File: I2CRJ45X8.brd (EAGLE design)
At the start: 80 x 50 mm, 51 parts, among them IC1 MCP23017SO, IC2 MCP23017SO, J1 M06-SOCKET, J2 M06-SOCKET, J3 M02X3-PIN, J4 M02X3-PIN

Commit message: Board and schematic labelling
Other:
- board text added: "!INT"
- board text added: "(C)2019 SuperHouse Automation Pty Ltd Released under the terms of the TAPR Open Hardware License: www.tapr.org/OHL"
- board text added: "1: Data 1 2: Data 2 3: Data 3 4: VIN 5: VIN 6: Data 4 7: GND 8: GND"
- board text added: "1K in series with data lines"
- board text added: "8 Channel I2C RJ45 Breakout"
- board text added: "RJ45 Pinout"
- board text added: "Super House"
- board text added: "VCC:1.8-5.5V VIN:12V I2C Addr: 0x20-0x27"
- board text added: "by Jon Oxer"
- board text added: "superhouse.tv"
- board text added: "www.superhouse.tv/i2crj45x8"
- board text removed: "(C)2019 SuperHouse Automation Pty Ltd"
- board text removed: "INT"
- board text removed: "www.superhouse.tv/switchcontroller"
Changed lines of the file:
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@@
 <?xml version="1.0" encoding="utf-8"?>
 <!DOCTYPE eagle SYSTEM "eagle.dtd">
-<eagle version="9.4.2">
+<eagle version="9.5.0">
 <drawing>
 <settings>
@@
 <wire x1="80" y1="3" x2="77" y2="0" width="0" layer="20" curve="-90"/>
 <wire x1="77" y1="0" x2="3" y2="0" width="0" layer="20"/>
-<text x="0.953" y="8.123" size="1.0668" layer="21" font="vector" ratio="17">v1.0</text>
-<text x="20.955" y="2.854" size="1.27" layer="21" font="vector" ratio="17">www.superhouse.tv/switchcontroller</text>
-<text x="20.471" y="9.096" size="1.016" layer="21" font="vector" ratio="15" rot="SR0">(C)2019 SuperHouse Automation Pty Ltd</text>
-<text x="1.191" y="6.171" size="0.8128" layer="21" font="vector" ratio="17">SKU: I2CRJ45X8</text>
+<text x="71.953" y="4.123" size="1.0668" layer="21" font="vector" ratio="17">v1.0</text>
+<text x="17.5" y="48.6" size="1.016" layer="21" font="vector" ratio="17">www.superhouse.tv/i2crj45x8</text>
+<text x="61.471" y="1.096" size="1.27" layer="22" font="vector" ratio="15" rot="SMR0">(C)2019 SuperHouse Automation Pty Ltd
+Released under the terms of
+the TAPR Open Hardware License:
+www.tapr.org/OHL</text>
+<text x="7.829" y="2.191" size="1.016" layer="21" font="vector" ratio="17" rot="R90">SKU: I2CRJ45X8</text>
 <hole x="3" y="3" drill="3.2"/>
 <hole x="77" y="3" drill="3.2"/>
@@
 <text x="3.7" y="22.38" size="1.778" layer="21" font="vector" ratio="18" align="center-left">GND</text>
 <text x="3.7" y="19.84" size="1.778" layer="21" font="vector" ratio="18" align="center-left">VIN</text>
-<text x="3.7" y="17.3" size="1.778" layer="21" font="vector" ratio="18" align="center-left">INT</text>
+<text x="3.7" y="17.3" size="1.778" layer="21" font="vector" ratio="18" align="center-left">!INT</text>
 <text x="76.7" y="30" size="1.778" layer="21" font="vector" ratio="18" align="center-right">SDA</text>
 <text x="76.7" y="27.46" size="1.778" layer="21" font="vector" ratio="18" align="center-right">SCL</text>
@@
 <text x="76.7" y="22.38" size="1.778" layer="21" font="vector" ratio="18" align="center-right">GND</text>
 <text x="76.7" y="19.84" size="1.778" layer="21" font="vector" ratio="18" align="center-right">VIN</text>
-<text x="76.7" y="17.3" size="1.778" layer="21" font="vector" ratio="18" align="center-right">INT</text>
+<text x="76.7" y="17.3" size="1.778" layer="21" font="vector" ratio="18" align="center-right">!INT</text>
 <text x="75" y="13" size="1.27" layer="21" font="vector" ratio="18" align="center-left">VIN</text>
 <text x="75" y="10" size="1.27" layer="21" font="vector" ratio="18" align="center-left">VCC</text>
@@
 <wire x1="79" y1="10" x2="78" y2="11" width="0.254" layer="21" curve="90"/>
 <wire x1="78" y1="11" x2="72" y2="11" width="0.254" layer="21"/>
+<text x="30" y="26" size="1.6764" layer="22" font="vector" ratio="12" rot="MR0">1: Data 1
+2: Data 2
+3: Data 3
+4: VIN
+5: VIN
+6: Data 4
+7: GND
+8: GND</text>
+<text x="31.8" y="46" size="1.6764" layer="22" font="vector" ratio="16" rot="MR0">RJ45 Pinout</text>
+<wire x1="31" y1="49" x2="33" y2="47" width="0.254" layer="22" curve="-90"/>
+<wire x1="33" y1="47" x2="33" y2="27" width="0.254" layer="22"/>
+<wire x1="33" y1="27" x2="31" y2="25" width="0.254" layer="22" curve="-90"/>
+<wire x1="31" y1="25" x2="17" y2="25" width="0.254" layer="22"/>
+<wire x1="17" y1="25" x2="15" y2="27" width="0.254" layer="22" curve="-90"/>
+<wire x1="15" y1="47" x2="17" y2="49" width="0.254" layer="22" curve="-90"/>
+<wire x1="17" y1="49" x2="31" y2="49" width="0.254" layer="22"/>
+<wire x1="15" y1="47" x2="15" y2="27" width="0.254" layer="22"/>
+<text x="64.529" y="25.096" size="1.27" layer="22" font="vector" ratio="15" rot="SMR0">1K in series with data lines</text>
+<text x="62.955" y="43.2" size="1.6" layer="21" font="vector" ratio="17" distance="30">8 Channel
+I2C RJ45
+Breakout</text>
+<text x="63.955" y="42" size="1.016" layer="21" font="vector" ratio="17">by Jon Oxer</text>
+<wire x1="42.426" y1="37.178" x2="41.402" y2="35.376" width="0.254" layer="21" curve="309.2564"/>
+<wire x1="42.426" y1="37.178" x2="41.04" y2="36.716" width="0.254" layer="21" curve="-163.361194"/>
+<wire x1="41.04" y1="36.716" x2="41.3" y2="38.464" width="0.254" layer="21"/>
+<wire x1="40.832" y1="35.946" x2="38.822" y2="35.946" width="0.254" layer="21"/>
+<wire x1="38.822" y1="35.946" x2="39.184" y2="38.102" width="0.254" layer="21"/>
+<wire x1="41.456" y1="37.648" x2="38.522" y2="37.648" width="0.254" layer="21"/>
+<wire x1="38.522" y1="37.648" x2="40.216" y2="38.926" width="0.254" layer="21"/>
+<wire x1="40.216" y1="38.926" x2="41.456" y2="37.648" width="0.254" layer="21"/>
+<wire x1="38.9" y1="37.8" x2="41" y2="37.8" width="0.254" layer="21"/>
+<wire x1="41" y1="37.8" x2="40.6" y2="38.2" width="0.254" layer="21"/>
+<wire x1="40.6" y1="38.2" x2="40.2" y2="38.6" width="0.254" layer="21"/>
+<wire x1="40.2" y1="38.6" x2="40.2" y2="38.7" width="0.254" layer="21"/>
+<wire x1="39.2" y1="38" x2="40.7" y2="38" width="0.254" layer="21"/>
+<wire x1="40.6" y1="38.2" x2="39.4" y2="38.2" width="0.254" layer="21"/>
+<wire x1="39.6" y1="38.4" x2="40.3" y2="38.4" width="0.254" layer="21"/>
+<wire x1="39.9" y1="38.6" x2="40.1" y2="38.6" width="0.254" layer="21"/>
+<text x="40" y="31" size="1.6" layer="21" font="vector" ratio="17" distance="20" align="bottom-center">Super
+House</text>
+<text x="40" y="28.5" size="1.016" layer="21" font="vector" ratio="17" distance="20" align="bottom-center">superhouse.tv</text>
+<text x="4.16" y="32.7" size="1.27" layer="21" font="vector" ratio="18" rot="R90" align="center-left">VCC:1.8-5.5V
+VIN:12V
+I2C Addr:
+0x20-0x27</text>
 </plain>
 <attributes>
@@
 </drawing>
 <compatibility>
+<note version="6.3" minversion="6.2.2" severity="warning">
+Since Version 6.2.2 text objects can contain more than one line,
+which will not be processed correctly with this version.
+</note>
 <note version="8.2" severity="warning">
 Since Version 8.2, EAGLE supports online libraries. The ids

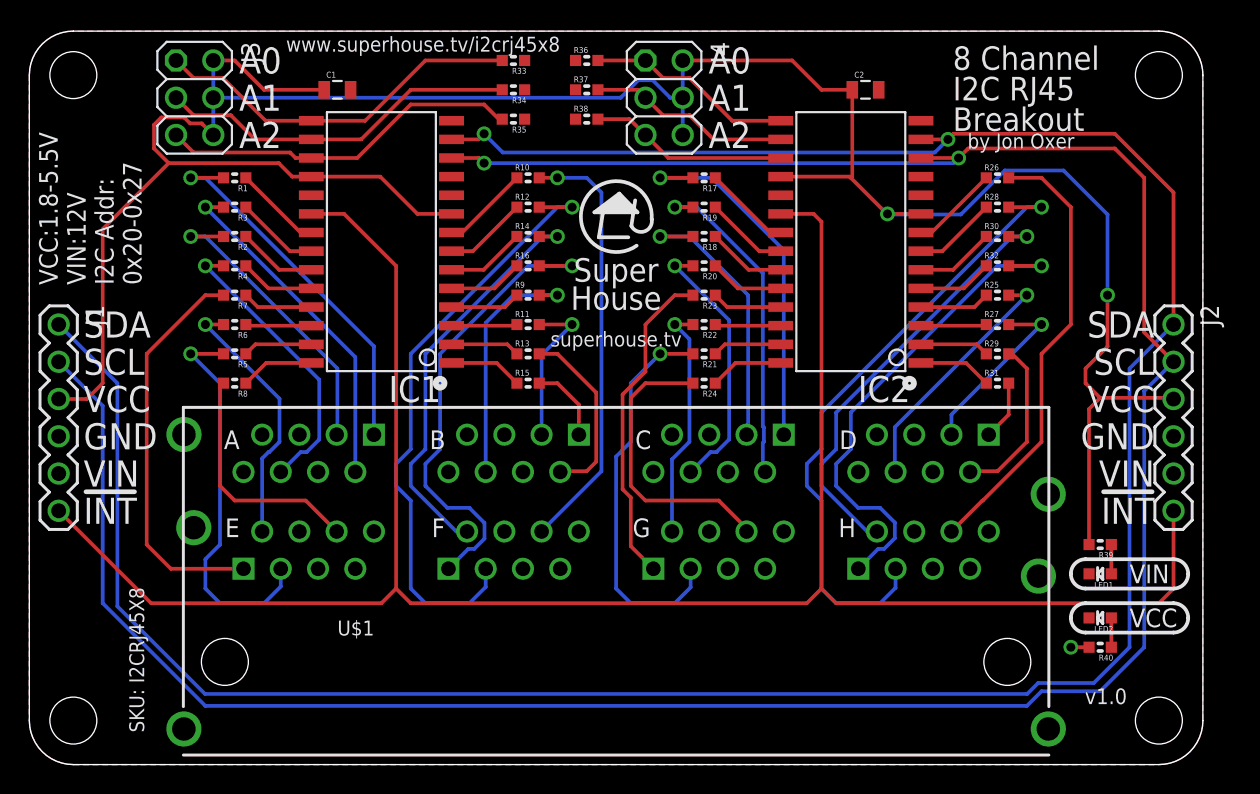
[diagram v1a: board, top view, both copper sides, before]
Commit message: Routing, Silkscreen Updated
Routed VIN, changed silkscreen for VCC and VIN LEDS to match corrent circuit
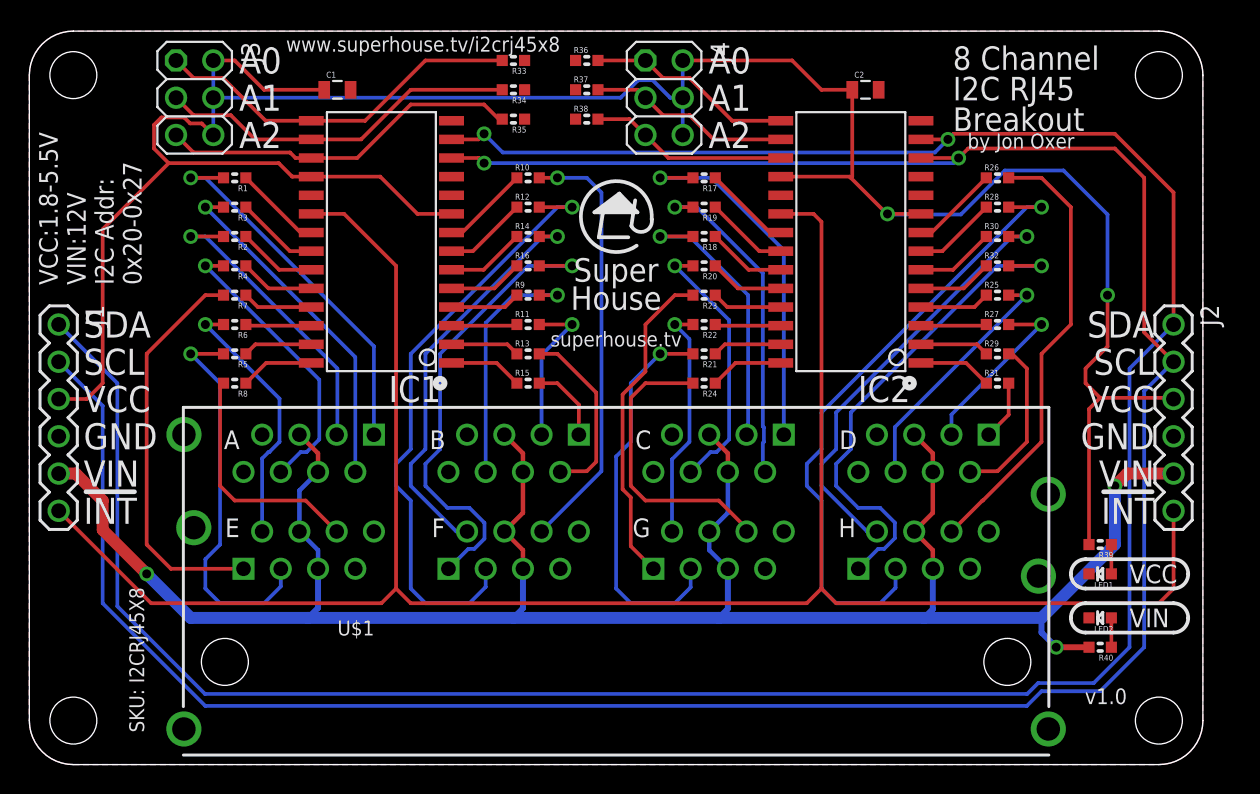
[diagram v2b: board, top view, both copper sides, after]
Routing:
- net VIN: track 1.24 -> 149.6 mm, vias 1 -> 3
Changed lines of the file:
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@@
 <drawing>
 <settings>
-<setting alwaysvectorfont="no"/>
+<setting alwaysvectorfont="yes"/>
 <setting keepoldvectorfont="yes"/>
 <setting verticaltext="up"/>
@@
 <text x="76.7" y="19.84" size="1.778" layer="21" font="vector" ratio="18" align="center-right">VIN</text>
 <text x="76.7" y="17.3" size="1.778" layer="21" font="vector" ratio="18" align="center-right">!INT</text>
-<text x="75" y="13" size="1.27" layer="21" font="vector" ratio="18" align="center-left">VIN</text>
-<text x="75" y="10" size="1.27" layer="21" font="vector" ratio="18" align="center-left">VCC</text>
+<text x="75" y="10" size="1.27" layer="21" font="vector" ratio="18" align="center-left">VIN</text>
+<text x="75" y="13" size="1.27" layer="21" font="vector" ratio="18" align="center-left">VCC</text>
 <wire x1="72" y1="14" x2="71" y2="13" width="0.254" layer="21" curve="90"/>
 <wire x1="71" y1="13" x2="72" y2="12" width="0.254" layer="21" curve="90"/>
@@
 <contactref element="J2" pad="5"/>
 <contactref element="R40" pad="2"/>
-<wire x1="72.238" y1="8" x2="71" y2="8" width="0.254" layer="1"/>
-<via x="71" y="8" extent="1-16" drill="0.6096"/>
-</signal>
-<signal name="GND">
+<wire x1="18.41" y1="22.49" x2="19.68" y2="21.22" width="0.3048" layer="1"/>
+<wire x1="19.68" y1="21.22" x2="19.68" y2="19.95" width="0.3048" layer="1"/>
+<wire x1="32.38" y1="22.49" x2="33.65" y2="21.22" width="0.3048" layer="1"/>
+<wire x1="33.65" y1="21.22" x2="33.65" y2="19.95" width="0.3048" layer="1"/>
+<wire x1="33.65" y1="19.95" x2="33.65" y2="17.16" width="0.3048" layer="1"/>
+<wire x1="33.65" y1="17.16" x2="32.38" y2="15.89" width="0.3048" layer="1"/>
+<wire x1="32.38" y1="15.89" x2="33.65" y2="14.62" width="0.3048" layer="1"/>
+<wire x1="33.65" y1="14.62" x2="33.65" y2="13.35" width="0.3048" layer="1"/>
+<wire x1="46.35" y1="22.49" x2="47.62" y2="21.22" width="0.3048" layer="1"/>
+<wire x1="47.62" y1="21.22" x2="47.62" y2="19.95" width="0.3048" layer="1"/>
+<wire x1="60.32" y1="22.49" x2="61.59" y2="21.22" width="0.3048" layer="1"/>
+<wire x1="61.59" y1="21.22" x2="61.59" y2="19.95" width="0.3048" layer="1"/>
+<wire x1="61.59" y1="19.95" x2="61.59" y2="17.16" width="0.3048" layer="1"/>
+<wire x1="61.59" y1="17.16" x2="60.32" y2="15.89" width="0.3048" layer="1"/>
+<wire x1="60.32" y1="15.89" x2="61.59" y2="14.62" width="0.3048" layer="1"/>
+<wire x1="61.59" y1="14.62" x2="61.59" y2="13.35" width="0.3048" layer="1"/>
+<wire x1="19.68" y1="19.95" x2="18.41" y2="18.68" width="0.3048" layer="16"/>
+<wire x1="18.41" y1="18.68" x2="18.41" y2="15.89" width="0.3048" layer="16"/>
+<wire x1="18.41" y1="15.89" x2="19.68" y2="14.62" width="0.3048" layer="16"/>
+<wire x1="19.68" y1="14.62" x2="19.68" y2="13.35" width="0.3048" layer="16"/>
+<wire x1="47.62" y1="19.95" x2="47.62" y2="17.16" width="0.3048" layer="16"/>
+<wire x1="47.62" y1="17.16" x2="46.35" y2="15.89" width="0.3048" layer="16"/>
+<wire x1="46.35" y1="15.89" x2="46.35" y2="14.62" width="0.3048" layer="16"/>
+<wire x1="46.35" y1="14.62" x2="47.62" y2="13.35" width="0.3048" layer="16"/>
+<wire x1="11" y1="10" x2="19" y2="10" width="0.8128" layer="16"/>
+<wire x1="19" y1="10" x2="33" y2="10" width="0.8128" layer="16"/>
+<wire x1="33" y1="10" x2="47" y2="10" width="0.8128" layer="16"/>
+<wire x1="47" y1="10" x2="61" y2="10" width="0.8128" layer="16"/>
+<wire x1="61" y1="10" x2="69" y2="10" width="0.8128" layer="16"/>
+<wire x1="11" y1="10" x2="8" y2="13" width="0.8128" layer="16"/>
+<via x="8" y="13" extent="1-16" drill="0.6096"/>
+<wire x1="8" y1="13" x2="5" y2="16" width="0.8128" layer="1"/>
+<wire x1="5" y1="16" x2="5" y2="18" width="0.8128" layer="1"/>
+<wire x1="5" y1="18" x2="3.16" y2="19.84" width="0.8128" layer="1"/>
+<wire x1="3.16" y1="19.84" x2="2" y2="19.84" width="0.8128" layer="1"/>
+<wire x1="69" y1="10" x2="74" y2="15" width="0.8128" layer="16"/>
+<wire x1="74" y1="15" x2="74" y2="19" width="0.8128" layer="16"/>
+<via x="74" y="19" extent="1-16" drill="0.6096"/>
+<wire x1="74" y1="19" x2="74.84" y2="19.84" width="0.8128" layer="1"/>
+<wire x1="74.84" y1="19.84" x2="78" y2="19.84" width="0.8128" layer="1"/>
+<wire x1="72.238" y1="8" x2="70" y2="8" width="0.4064" layer="1"/>
+<via x="70" y="8" extent="1-16" drill="0.6096"/>
+<wire x1="70" y1="8" x2="69" y2="9" width="0.4064" layer="16"/>
+<wire x1="69" y1="9" x2="69" y2="10" width="0.4064" layer="16"/>
+<wire x1="61.59" y1="13.35" x2="61.59" y2="10.59" width="0.4064" layer="16"/>
+<wire x1="61.59" y1="10.59" x2="61" y2="10" width="0.4064" layer="16"/>
+<wire x1="47.62" y1="13.35" x2="47.62" y2="10.62" width="0.4064" layer="16"/>
+<wire x1="47.62" y1="10.62" x2="47" y2="10" width="0.4064" layer="16"/>
+<wire x1="33.65" y1="13.35" x2="33.65" y2="10.65" width="0.4064" layer="16"/>
+<wire x1="33.65" y1="10.65" x2="33" y2="10" width="0.4064" layer="16"/>
+<wire x1="19.68" y1="13.35" x2="19.68" y2="10.68" width="0.4064" layer="16"/>
+<wire x1="19.68" y1="10.68" x2="19" y2="10" width="0.4064" layer="16"/>
+</signal>
+<signal name="GND" airwireshidden="yes">
 <polygon width="0.4064" layer="1">
 <vertex x="77" y="0" curve="90"/>
@@
 <contactref element="LED1" pad="C"/>
 <contactref element="LED2" pad="C"/>
+<wire x1="60.78" y1="38.81" x2="57.9" y2="46" width="0" layer="19" extent="1-1"/>
+<wire x1="57.78" y1="22.49" x2="60.78" y2="38.81" width="0" layer="19" extent="1-1"/>
+<wire x1="56.51" y1="19.95" x2="57.78" y2="22.49" width="0" layer="19" extent="1-1"/>
+<wire x1="51.43" y1="15.89" x2="56.51" y2="19.95" width="0" layer="19" extent="1-1"/>
+<wire x1="50.16" y1="13.35" x2="51.43" y2="15.89" width="0" layer="19" extent="1-1"/>
+<wire x1="65.4" y1="15.89" x2="56.51" y2="19.95" width="0" layer="19" extent="1-1"/>
+<wire x1="64.13" y1="13.35" x2="65.4" y2="15.89" width="0" layer="19" extent="1-1"/>
+<wire x1="72.238" y1="13" x2="65.4" y2="15.89" width="0" layer="19" extent="1-1"/>
+<wire x1="72.238" y1="10" x2="72.238" y2="13" width="0" layer="19" extent="1-1"/>
+<wire x1="42.54" y1="19.95" x2="51.43" y2="15.89" width="0" layer="19" extent="1-1"/>
+<wire x1="43.81" y1="22.49" x2="42.54" y2="19.95" width="0" layer="19" extent="1-1"/>
+<wire x1="37.46" y1="15.89" x2="42.54" y2="19.95" width="0" layer="19" extent="1-1"/>
+<wire x1="36.19" y1="13.35" x2="37.46" y2="15.89" width="0" layer="19" extent="1-1"/>
+<wire x1="28.57" y1="19.95" x2="37.46" y2="15.89" width="0" layer="19" extent="1-1"/>
+<wire x1="29.84" y1="22.49" x2="28.57" y2="19.95" width="0" layer="19" extent="1-1"/>
+<wire x1="23.49" y1="15.89" x2="28.57" y2="19.95" width="0" layer="19" extent="1-1"/>
+<wire x1="22.22" y1="13.35" x2="23.49" y2="15.89" width="0" layer="19" extent="1-1"/>
+<wire x1="14.6" y1="19.95" x2="23.49" y2="15.89" width="0" layer="19" extent="1-1"/>
+<wire x1="15.87" y1="22.49" x2="14.6" y2="19.95" width="0" layer="19" extent="1-1"/>
+<wire x1="78" y1="22.38" x2="72.238" y2="13" width="0" layer="19" extent="1-1"/>
+<wire x1="2" y1="22.38" x2="14.6" y2="19.95" width="0" layer="19" extent="1-1"/>
+<wire x1="28.78" y1="38.81" x2="29.84" y2="22.49" width="0" layer="19" extent="1-1"/>
+<wire x1="33.762" y1="44" x2="28.78" y2="38.81" width="0" layer="19" extent="1-1"/>
+<wire x1="33.762" y1="46" x2="33.762" y2="44" width="0" layer="19" extent="1-1"/>
+<wire x1="33.762" y1="48" x2="33.762" y2="46" width="0" layer="19" extent="1-1"/>
+<wire x1="37.238" y1="48" x2="33.762" y2="48" width="0" layer="19" extent="1-1"/>
+<wire x1="37.238" y1="46" x2="37.238" y2="48" width="0" layer="19" extent="1-1"/>
+<wire x1="37.238" y1="44" x2="37.238" y2="46" width="0" layer="19" extent="1-1"/>
+<wire x1="21.9" y1="46" x2="28.78" y2="38.81" width="0" layer="19" extent="1-1"/>
 </signal>
 <signal name="GPB6">
@@
 <wire x1="12" y1="4" x2="68" y2="4" width="0.254" layer="16"/>
 <wire x1="76" y1="8" x2="76" y2="25.46" width="0.254" layer="16"/>
-</signal>
-<signal name="GND0">
-<contactref element="U$1" pad="GND0"/>
 </signal>
 <signal name="GND1">
@@
 <wire x1="73.762" y1="10" x2="73.762" y2="8" width="0.254" layer="1"/>
 </signal>
+<signal name="GND0">
+<contactref element="U$1" pad="GND0"/>
+</signal>
 </signals>
